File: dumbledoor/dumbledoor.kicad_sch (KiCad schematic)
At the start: 20 parts, among them Q1 AO3400A, Q2 AO3400A, Q3 IRLZ24, U2 TLP627

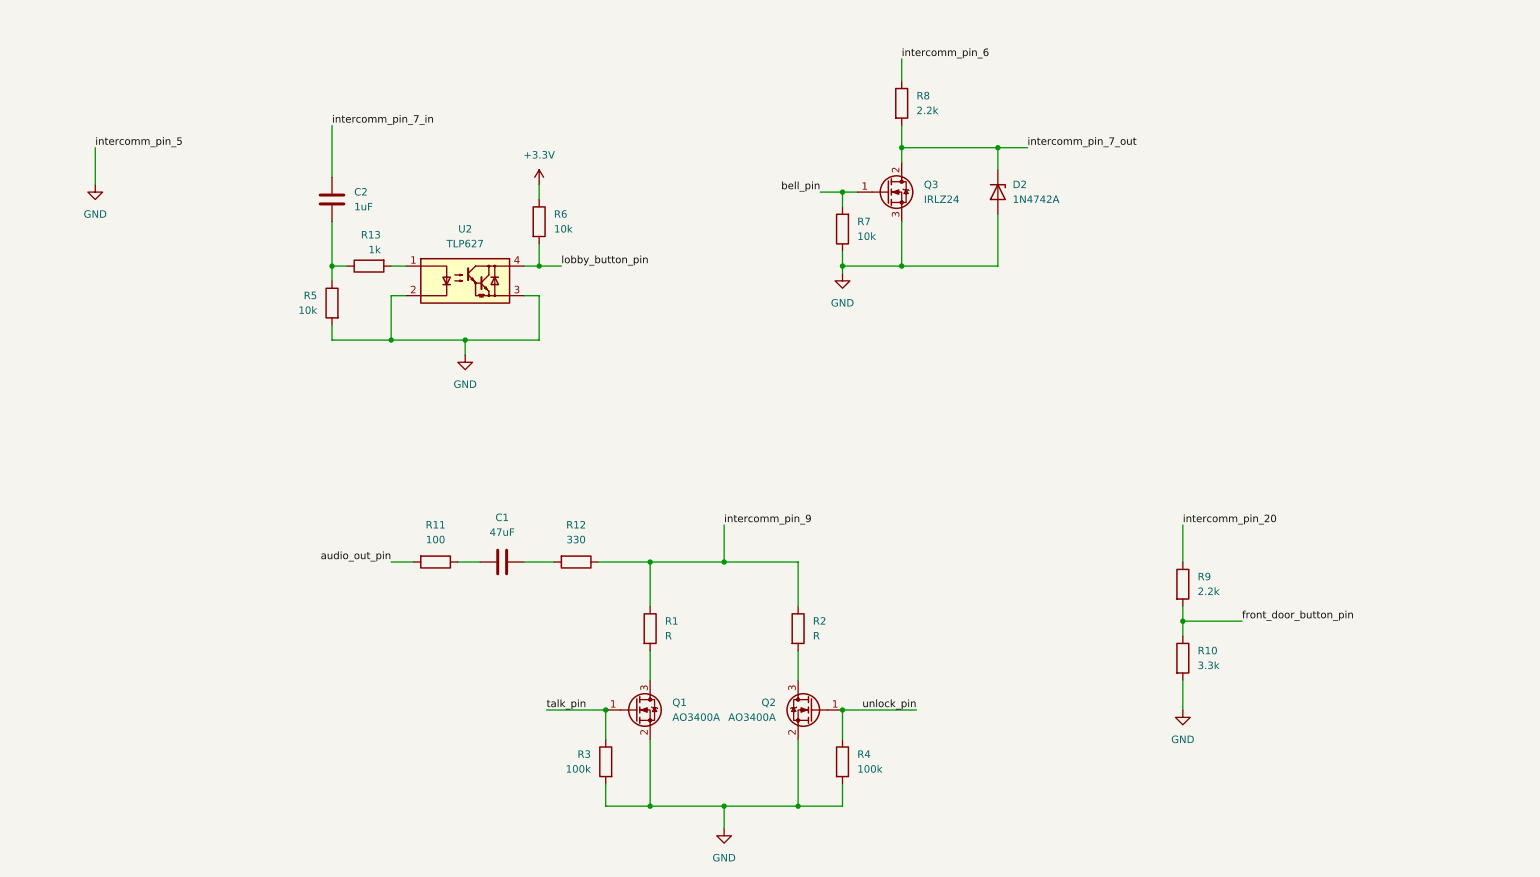
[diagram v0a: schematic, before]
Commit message: Schematic: KiCad 10, input and bell stage changes
Co-Authored-By: Claude Opus 5.5 <noreply@anthropic.com>
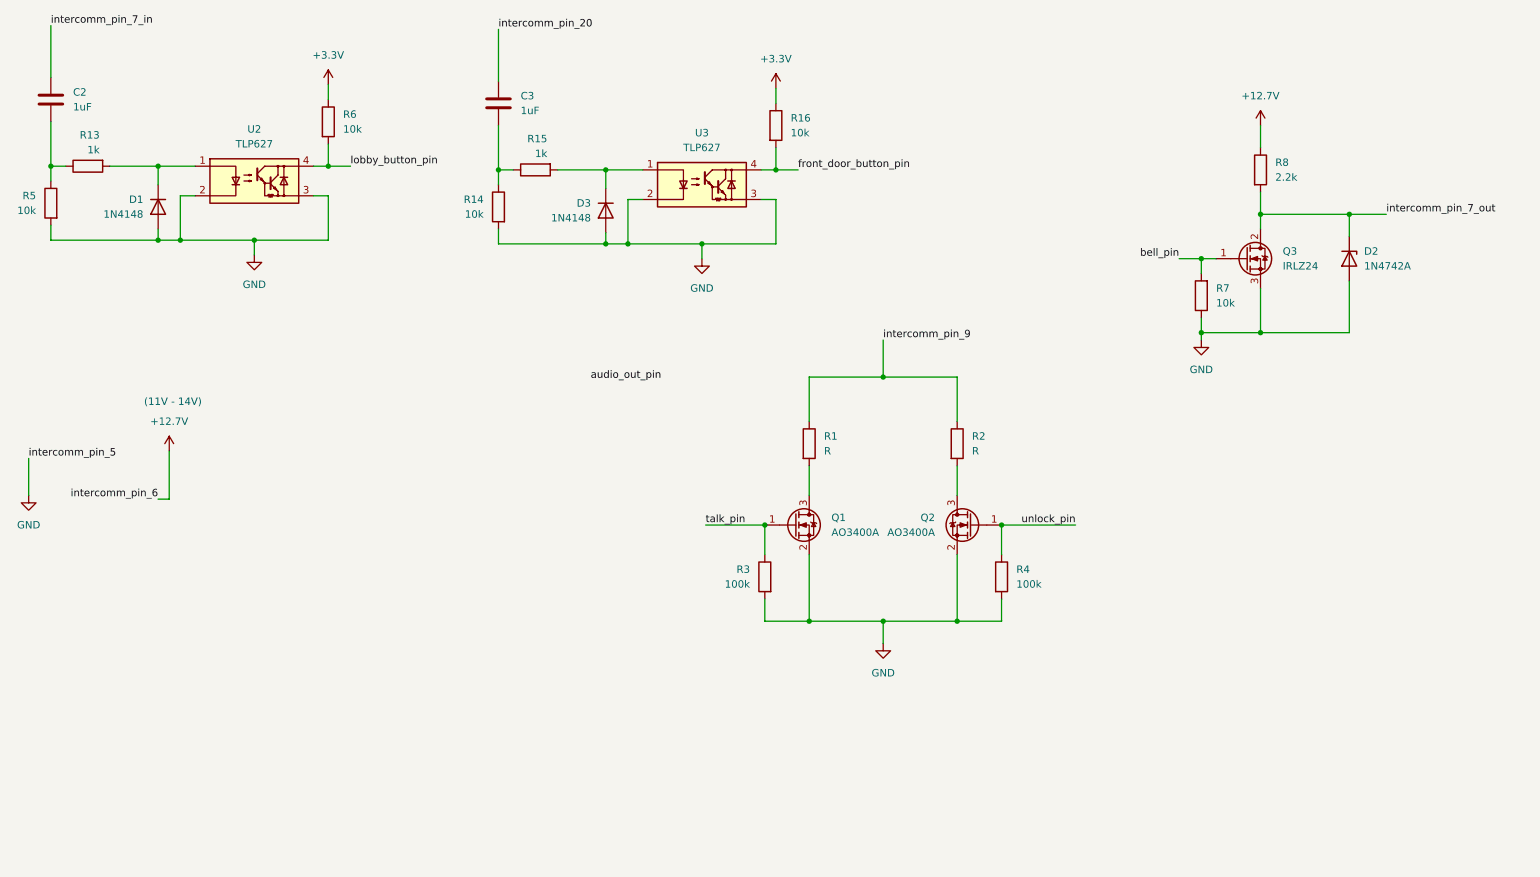
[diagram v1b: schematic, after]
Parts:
- removed C1: 47uF, symbol Device:C
- removed R10: 3.3k, symbol Device:R
- removed R11: 100, symbol Device:R
- removed R12: 330, symbol Device:R
- removed R9: 2.2k, symbol Device:R
- added C3: 1uF, symbol Device:C
- added D1, D3: 1N4148, Diode_THT:D_DO-35_SOD27_P7.62mm_Horizontal, symbol Diode:1N4148
- added R14, R16: 10k, symbol Device:R
- added R15: 1k, symbol Device:R
- added U3: TLP627, Package_DIP:DIP-4_W7.62mm, symbol Isolator:TLP627
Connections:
- net +3.3V: now also R16.1
- net GND: now also D1.2 (A), D3.2 (A), R14.2, U3.2, U3.3
- net front_door_button_pin: now also R16.2, U3.4
- net intercomm_pin_20: now also C3.1
- net at R13.2, U2.1: now also D1.1 (K)
- net intercomm_pin_6 renamed +12.7V
- new net: D3.1 (K), R15.2, U3.1
- new net: C3.2, R14.1, R15.1
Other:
- note added: "(11V - 14V)"
- moved on the sheet: C2, D2, Q1, Q2, Q3, R1, R13, R2, R3, R4, R5, R6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
